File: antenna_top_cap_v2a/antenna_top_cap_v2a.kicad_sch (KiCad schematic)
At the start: 31 parts, among them J1 DEBUG, J12 USB_C_Receptacle_USB2.0_16P, J2 Battery Charge Bypass, J3 FC Reset Jumper, J4 FC USB Bootselect Jumper, J5 Conn_Coaxial, Q1 BSS138, U1 VL6180XV0NR/1, U16 MCP9808T-E/MS, U2 LP5907-2.8V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

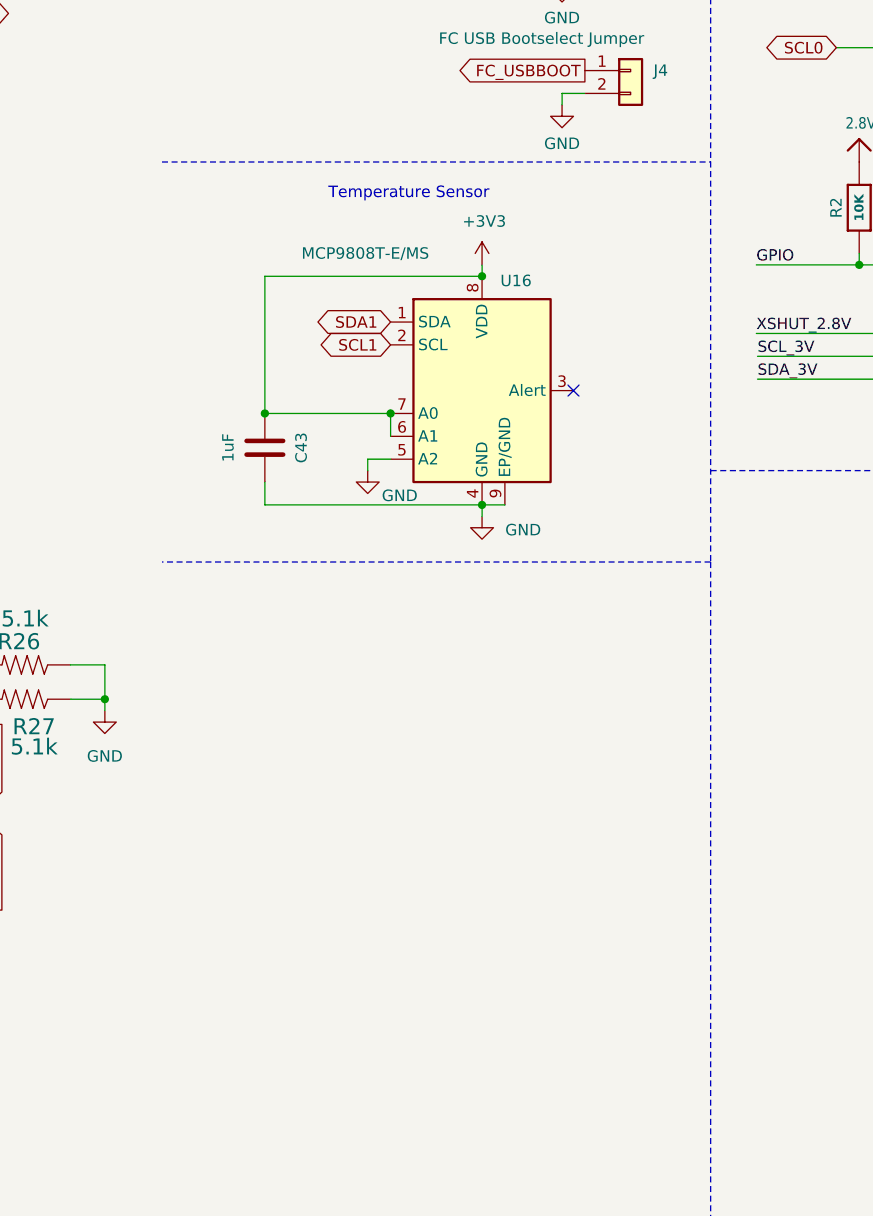
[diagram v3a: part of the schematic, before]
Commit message: Added VEML7700 Light Sensor
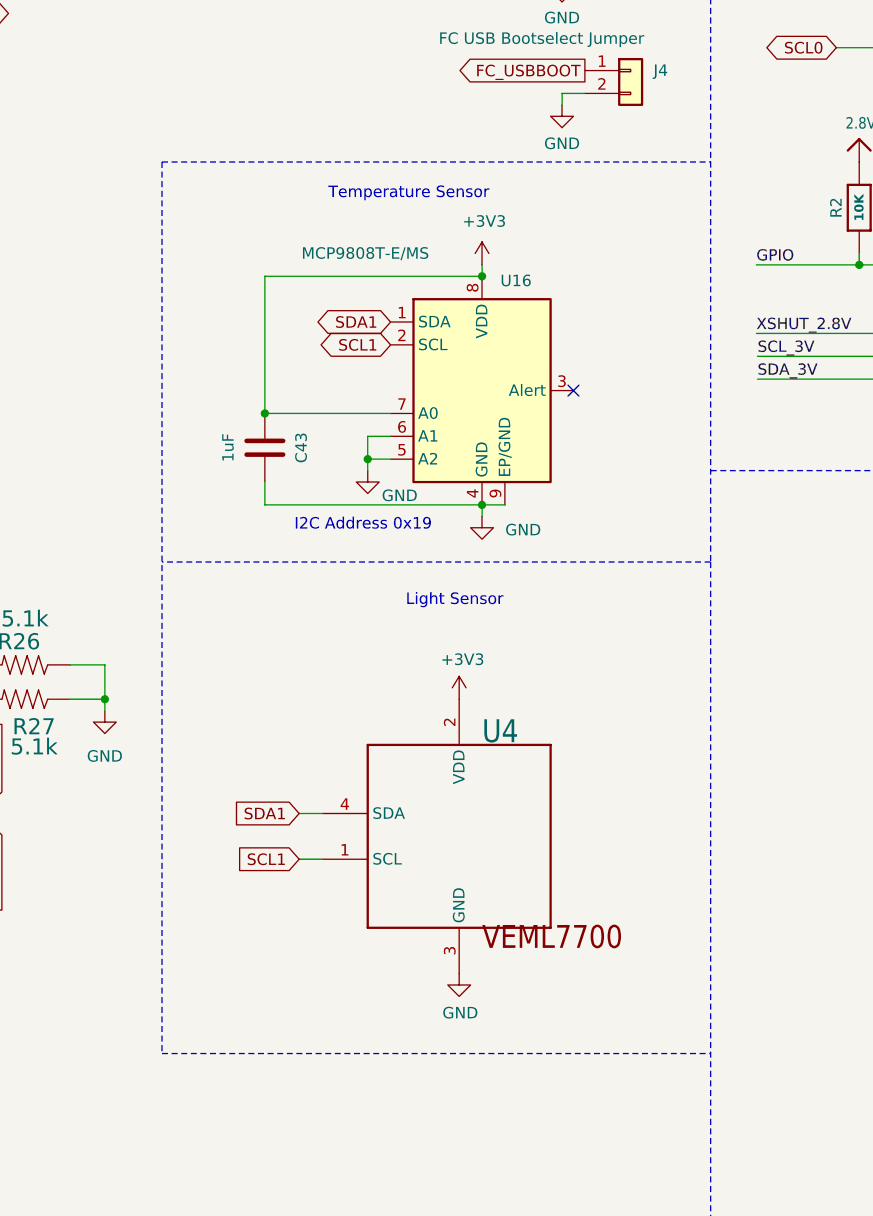
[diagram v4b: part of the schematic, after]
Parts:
- added U4: VEML7700, VEML7700-TT:XDCR_VEML7700-TT, symbol Adafruit VEML7700-eagle-import:VEML7700
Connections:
- net +3V3: now also U4.2 (VDD); no longer U16.6 (A1)
- net GND: now also U16.6 (A1), U4.3 (GND)
- net SCL0: now also U4.1 (SCL)
- net SDA0: now also U4.4 (SDA)
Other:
- note added: "I2C Address 0x19"
- note added: "Light Sensor"

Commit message: Production Files as Ordered 4/17/2025
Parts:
- removed U3: NCS1.5-232+, RF_Converter:Balun_Johanson_0896BM15A0001, symbol Transformer:0433BM15A0001
- added U5: HHM1591D1, easyeda2kicad:XFMR-SMD_HHM1591D1, symbol easyeda2kicad:HHM1591D1
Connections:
- net GND: now also U5.2 (GND), U5.5 (GND)
- net at J6.1 (tape_1): now also U5.3 (Balancedport)
- net at J6.2 (tape_2): now also U5.4 (Balancedport)
- net at J5.1 (In): now also U5.1 (Unbalancedport)
- no-connect marks 12 -> 13
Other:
- moved on the sheet: J5, J6
